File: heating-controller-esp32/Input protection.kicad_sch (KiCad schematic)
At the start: 2 parts

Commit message: Initial design of schematic complete. Started laying out PCB
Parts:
- renumbered D5 to D1, R26 to R14
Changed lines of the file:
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@@
   (symbol (lib_id "Diode:BAS40-04") (at 91.44 69.85 90) (unit 1)
     (in_bom yes) (on_board yes)
-    (property "Reference" "D5" (id 0) (at 86.6902 68.6816 90)
+    (property "Reference" "D1" (id 0) (at 86.6902 68.6816 90)
       (effects (font (size 1.27 1.27)) (justify left))
     )
@@
   (symbol (lib_id "Device:R") (at 101.6 69.85 270) (unit 1)
     (in_bom yes) (on_board yes)
-    (property "Reference" "R26" (id 0) (at 101.6 64.5922 90))
+    (property "Reference" "R14" (id 0) (at 101.6 64.5922 90))
     (property "Value" "~" (id 1) (at 101.6 66.9036 90))
     (property "Footprint" "Resistor_SMD:R_0603_1608Metric" (id 2) (at 101.6 68.072 90)
@@
   (symbol (lib_id "power:GND") (at 88.9 77.47 0) (unit 1)
     (in_bom yes) (on_board yes)
-    (property "Reference" "#PWR0169" (id 0) (at 88.9 83.82 0)
+    (property "Reference" "#PWR0172" (id 0) (at 88.9 83.82 0)
       (effects (font (size 1.27 1.27)) hide)
     )

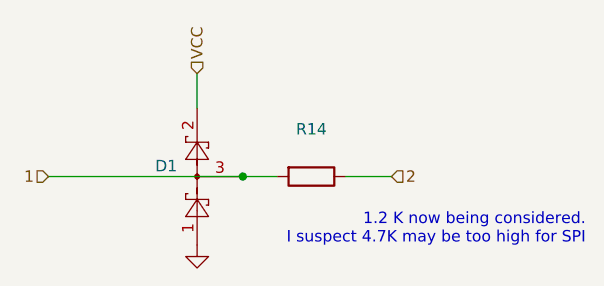
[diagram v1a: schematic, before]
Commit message: Changes for JLCB fabrication using https://github.com/Bouni/kicad-jlcpcb-tools
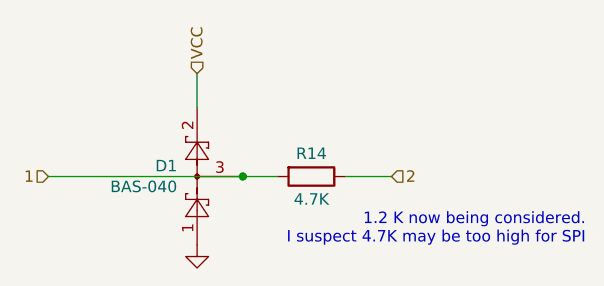
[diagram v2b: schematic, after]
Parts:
- D1: value ~ -> BAS-040
- R14: value ~ -> 4.7K
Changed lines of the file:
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@@
       (effects (font (size 1.27 1.27)) (justify left))
     )
-    (property "Value" "~" (id 1) (at 86.6902 70.993 90)
+    (property "Value" "BAS-040" (id 1) (at 86.6902 70.993 90)
       (effects (font (size 1.27 1.27)) (justify left))
     )
@@
   (symbol (lib_id "Device:R") (at 101.6 69.85 270) (unit 1)
     (in_bom yes) (on_board yes)
-    (property "Reference" "R14" (id 0) (at 101.6 64.5922 90))
-    (property "Value" "~" (id 1) (at 101.6 66.9036 90))
+    (property "Reference" "R14" (id 0) (at 101.6 67.31 90))
+    (property "Value" "4.7K" (id 1) (at 101.6 72.39 90))
     (property "Footprint" "Resistor_SMD:R_0603_1608Metric" (id 2) (at 101.6 68.072 90)
       (effects (font (size 1.27 1.27)) hide)
